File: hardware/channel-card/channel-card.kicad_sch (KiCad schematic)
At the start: 0 parts

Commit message: Add channel card input stage schematic and AD8273 symbol
- Input sheet: 10-pin input module header, input protection, AD8273
  receiver at G = 1/2 (wired inverting), AC coupling, NE5532 trim stage
  (-20 to +20 dB overall) with 6.2 V zener soft clip, 150 Hz 12 dB/oct
  Sallen-Key low-cut selected by a DG413, LOW-CUT button and LED.
  Netlist verified against the design; ERC clean apart from the sheet
  links to the not-yet-drawn filter sheet and the PGND label.
- Shared symbol library hardware/libs/syntsamix.kicad_sym with the
  AD8273 (pinout from datasheet Rev B), registered in both projects.
- Decision 69: buttons switch stereo audio through DG413 analog
  switches; a local +5 V supply feeds the switch logic.
- parts.csv: input stage parts; ROADMAP and CLAUDE.md updated for the
  schematic phase.

Co-Authored-By: Claude Opus 5.5 <noreply@anthropic.com>
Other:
- added sheet Input (input.kicad_sch)
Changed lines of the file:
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@@
 	(generator_version "10.0")
 	(paper "A4")
+	(sheet
+		(at 25.4 38.1)
+		(size 30.48 20.32)
+		(exclude_from_sim no)
+		(in_bom yes)
+		(on_board yes)
+		(dnp no)
+		(fields_autoplaced yes)
+		(stroke
+			(width 0.1524)
+			(type solid)
+		)
+		(fill
+			(color 0 0 0 0.0000)
+		)
+		(property "Sheetname" "Input"
+			(at 25.4 37.3884 0)
+			(effects
+				(font
+					(size 1.27 1.27)
+				)
+				(justify left bottom)
+			)
+		)
+		(property "Sheetfile" "input.kicad_sch"
+			(at 25.4 59.0046 0)
+			(effects
+				(font
+					(size 1.27 1.27)
+				)
+				(justify left top)
+			)
+		)
+		(pin "L_PREFILT" output
+			(at 55.88 40.64 0)
+			(effects
+				(font
+					(size 1.27 1.27)
+				)
+				(justify right)
+			)
+		)
+		(pin "R_PREFILT" output
+			(at 55.88 43.18 0)
+			(effects
+				(font
+					(size 1.27 1.27)
+				)
+				(justify right)
+			)
+		)
+		(instances
+			(project "channel-card"
+				(path "/44b8098e-8b91-4d90-8e36-746977844050"
+					(page "2")
+				)
+			)
+		)
+	)
 	(sheet_instances
 		(path "/"

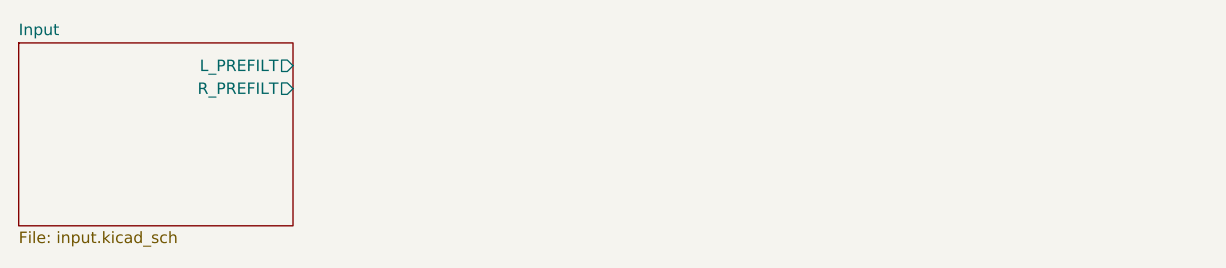
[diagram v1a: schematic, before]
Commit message: Add channel card filter sheet with LM13700 Q VCA
Two SSI2144 ladder filters with the datasheet's external Q VCA for
resonance compensation (jumper: none, half, full), shared cutoff summer
with CV input, drive jumpers and DG413 bypass. Adds the SSI2144 symbol,
decision 71, new part numbers, breadboard test 9 and a follow-up
Electrokit order.

Co-Authored-By: Claude Opus 5.5 <noreply@anthropic.com>
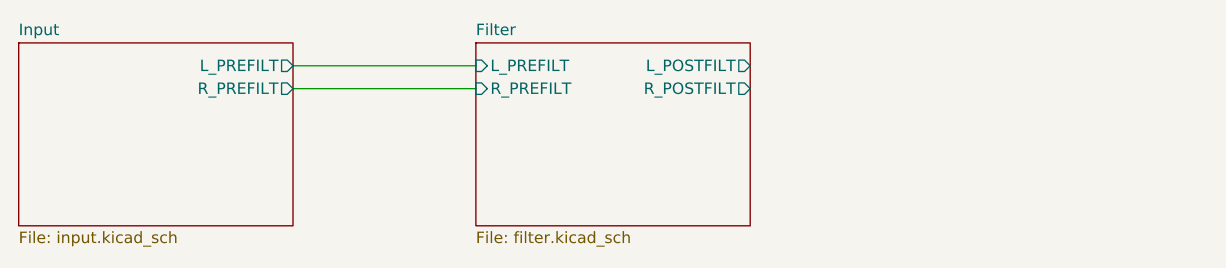
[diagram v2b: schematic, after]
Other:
- added sheet Filter (filter.kicad_sch)
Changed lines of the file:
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@@
 		)
 		(pin "L_PREFILT" output
-			(at 55.88 40.64 0)
+			(at 55.88 40.64 0.0000)
 			(effects
 				(font
@@
 		)
 		(pin "R_PREFILT" output
-			(at 55.88 43.18 0)
+			(at 55.88 43.18 0.0000)
 			(effects
 				(font
@@
 		)
 	)
+	(sheet
+		(at 76.2 38.1)
+		(size 30.48 20.32)
+		(exclude_from_sim no)
+		(in_bom yes)
+		(on_board yes)
+		(dnp no)
+		(fields_autoplaced yes)
+		(stroke
+			(width 0.1524)
+			(type solid)
+		)
+		(fill
+			(color 0 0 0 0.0000)
+		)
+		(property "Sheetname" "Filter"
+			(at 76.2 37.3884 0)
+			(effects
+				(font
+					(size 1.27 1.27)
+				)
+				(justify left bottom)
+			)
+		)
+		(property "Sheetfile" "filter.kicad_sch"
+			(at 76.2 59.0046 0)
+			(effects
+				(font
+					(size 1.27 1.27)
+				)
+				(justify left top)
+			)
+		)
+		(pin "L_PREFILT" input
+			(at 76.2 40.64 180)
+			(effects
+				(font
+					(size 1.27 1.27)
+				)
+				(justify left)
+			)
+		)
+		(pin "R_PREFILT" input
+			(at 76.2 43.18 180)
+			(effects
+				(font
+					(size 1.27 1.27)
+				)
+				(justify left)
+			)
+		)
+		(pin "L_POSTFILT" output
+			(at 106.68 40.64 0)
+			(effects
+				(font
+					(size 1.27 1.27)
+				)
+				(justify right)
+			)
+		)
+		(pin "R_POSTFILT" output
+			(at 106.68 43.18 0)
+			(effects
+				(font
+					(size 1.27 1.27)
+				)
+				(justify right)
+			)
+		)
+		(instances
+			(project "channel-card"
+				(path "/44b8098e-8b91-4d90-8e36-746977844050"
+					(page "2")
+				)
+			)
+		)
+	)
+	(wire (pts (xy 55.88 40.64) (xy 76.2 40.64)) (stroke (width 0) (type default)))
+	(wire (pts (xy 55.88 43.18) (xy 76.2 43.18)) (stroke (width 0) (type default)))
 	(sheet_instances
 		(path "/"

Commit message: Add channel card level sheet and sheet generator scripts
SSI2162 VCA with a 3-segment console fader law, click-free DG413 mute
and DUCK on SC_ENV (decision 72), SSI2162 symbol, fader-law breadboard
test and parts. The Filter and Level sheets are generated by scripts in
hardware/channel-card/scripts, with a netlist and duplicate-reference
check. In-file SPDX headers now take precedence over REUSE.toml.

Co-Authored-By: Claude Opus 5.5 <noreply@anthropic.com>
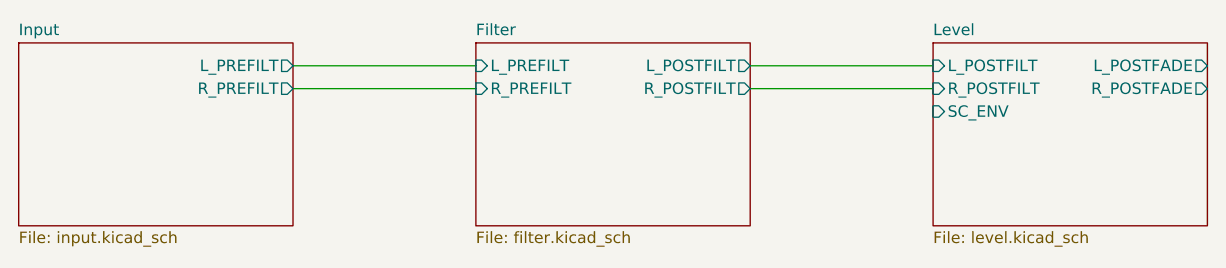
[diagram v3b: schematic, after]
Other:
- added sheet Level (level.kicad_sch)
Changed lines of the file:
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@@
 		)
 		(pin "L_POSTFILT" output
-			(at 106.68 40.64 0)
+			(at 106.68 40.64 0.0000)
 			(effects
 				(font
@@
 		)
 		(pin "R_POSTFILT" output
-			(at 106.68 43.18 0)
+			(at 106.68 43.18 0.0000)
 			(effects
 				(font
@@
 		)
 	)
-	(wire (pts (xy 55.88 40.64) (xy 76.2 40.64)) (stroke (width 0) (type default)))
-	(wire (pts (xy 55.88 43.18) (xy 76.2 43.18)) (stroke (width 0) (type default)))
+	(sheet
+		(at 127 38.1)
+		(size 30.48 20.32)
+		(exclude_from_sim no)
+		(in_bom yes)
+		(on_board yes)
+		(dnp no)
+		(fields_autoplaced yes)
+		(stroke
+			(width 0.1524)
+			(type solid)
+		)
+		(fill
+			(color 0 0 0 0.0000)
+		)
+		(property "Sheetname" "Level"
+			(at 127 37.3884 0)
+			(effects
+				(font
+					(size 1.27 1.27)
+				)
+				(justify left bottom)
+			)
+		)
+		(property "Sheetfile" "level.kicad_sch"
+			(at 127 59.0046 0)
+			(effects
+				(font
+					(size 1.27 1.27)
+				)
+				(justify left top)
+			)
+		)
+		(pin "L_POSTFILT" input
+			(at 127 40.64 180)
+			(effects
+				(font
+					(size 1.27 1.27)
+				)
+				(justify left)
+			)
+		)
+		(pin "R_POSTFILT" input
+			(at 127 43.18 180)
+			(effects
+				(font
+					(size 1.27 1.27)
+				)
+				(justify left)
+			)
+		)
+		(pin "SC_ENV" input
+			(at 127 45.72 180)
+			(effects
+				(font
+					(size 1.27 1.27)
+				)
+				(justify left)
+			)
+		)
+		(pin "L_POSTFADE" output
+			(at 157.48 40.64 0)
+			(effects
+				(font
+					(size 1.27 1.27)
+				)
+				(justify right)
+			)
+		)
+		(pin "R_POSTFADE" output
+			(at 157.48 43.18 0)
+			(effects
+				(font
+					(size 1.27 1.27)
+				)
+				(justify right)
+			)
+		)
+		(instances
+			(project "channel-card"
+				(path "/44b8098e-8b91-4d90-8e36-746977844050"
+					(page "2")
+				)
+			)
+		)
+	)
+	(wire
+		(pts (xy 55.88 40.64) (xy 76.2 40.64))
+		(stroke (width 0) (type solid))
+	)
+	(wire
+		(pts (xy 55.88 43.18) (xy 76.2 43.18))
+		(stroke (width 0) (type solid))
+	)
+	(wire (pts (xy 106.68 40.64) (xy 127 40.64)) (stroke (width 0) (type default)))
+	(wire (pts (xy 106.68 43.18) (xy 127 43.18)) (stroke (width 0) (type default)))
 	(sheet_instances
 		(path "/"
